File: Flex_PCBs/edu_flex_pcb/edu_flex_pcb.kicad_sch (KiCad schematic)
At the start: 2 parts, among them J1 Conn_01x22_Male, J2 Conn_01x22_Male

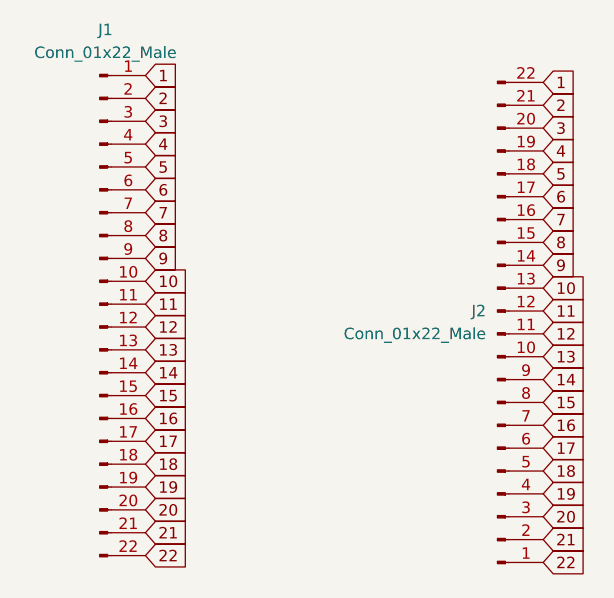
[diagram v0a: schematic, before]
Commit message: Added small modifications to the existing flex PCBs plus the new ones: Y- and X-.
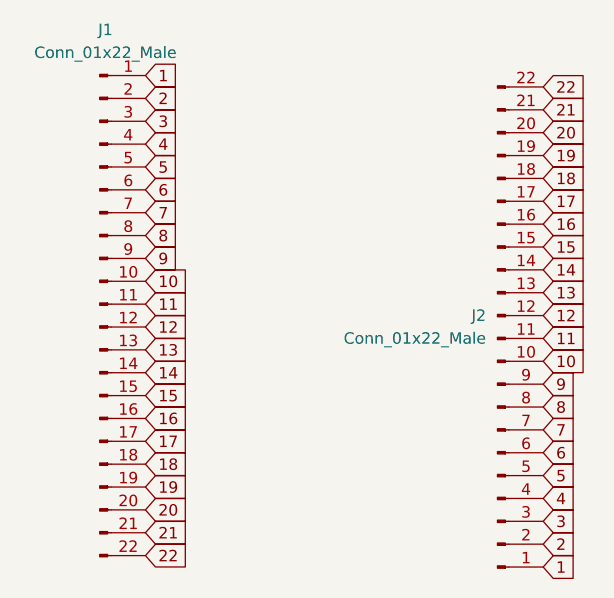
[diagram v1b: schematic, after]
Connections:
- net 1: now also J2.1 (Pin_1); no longer J2.22 (Pin_22)
- net 10: now also J2.10 (Pin_10); no longer J2.13 (Pin_13)
- net 11: now also J2.11 (Pin_11); no longer J2.12 (Pin_12)
- net 12: now also J2.12 (Pin_12); no longer J2.11 (Pin_11)
- net 13: now also J2.13 (Pin_13); no longer J2.10 (Pin_10)
- net 14: now also J2.14 (Pin_14); no longer J2.9 (Pin_9)
- net 15: now also J2.15 (Pin_15); no longer J2.8 (Pin_8)
- net 16: now also J2.16 (Pin_16); no longer J2.7 (Pin_7)
- net 17: now also J2.17 (Pin_17); no longer J2.6 (Pin_6)
- net 18: now also J2.18 (Pin_18); no longer J2.5 (Pin_5)
- net 19: now also J2.19 (Pin_19); no longer J2.4 (Pin_4)
- net 2: now also J2.2 (Pin_2); no longer J2.21 (Pin_21)
- net 20: now also J2.20 (Pin_20); no longer J2.3 (Pin_3)
- net 21: now also J2.21 (Pin_21); no longer J2.2 (Pin_2)
- net 22: now also J2.22 (Pin_22); no longer J2.1 (Pin_1)
- net 3: now also J2.3 (Pin_3); no longer J2.20 (Pin_20)
- net 4: now also J2.4 (Pin_4); no longer J2.19 (Pin_19)
- net 5: now also J2.5 (Pin_5); no longer J2.18 (Pin_18)
- net 6: now also J2.6 (Pin_6); no longer J2.17 (Pin_17)
- net 7: now also J2.7 (Pin_7); no longer J2.16 (Pin_16)
- net 8: now also J2.8 (Pin_8); no longer J2.15 (Pin_15)
- net 9: now also J2.9 (Pin_9); no longer J2.14 (Pin_14)
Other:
- moved on the sheet: J2
